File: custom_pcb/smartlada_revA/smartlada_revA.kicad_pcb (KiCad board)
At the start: 2 copper layers, 80 x 65 mm, 34 parts, among them J1 +12V IN, J2 LAMPS_OUT, J3 DEVBOARD PINS, Q1 AOD4184A, Q2 AOD4184A, Q3 AOD4184A, Q4 AOD4184A, Q5 AOD4185, U1 TPS54202DDC

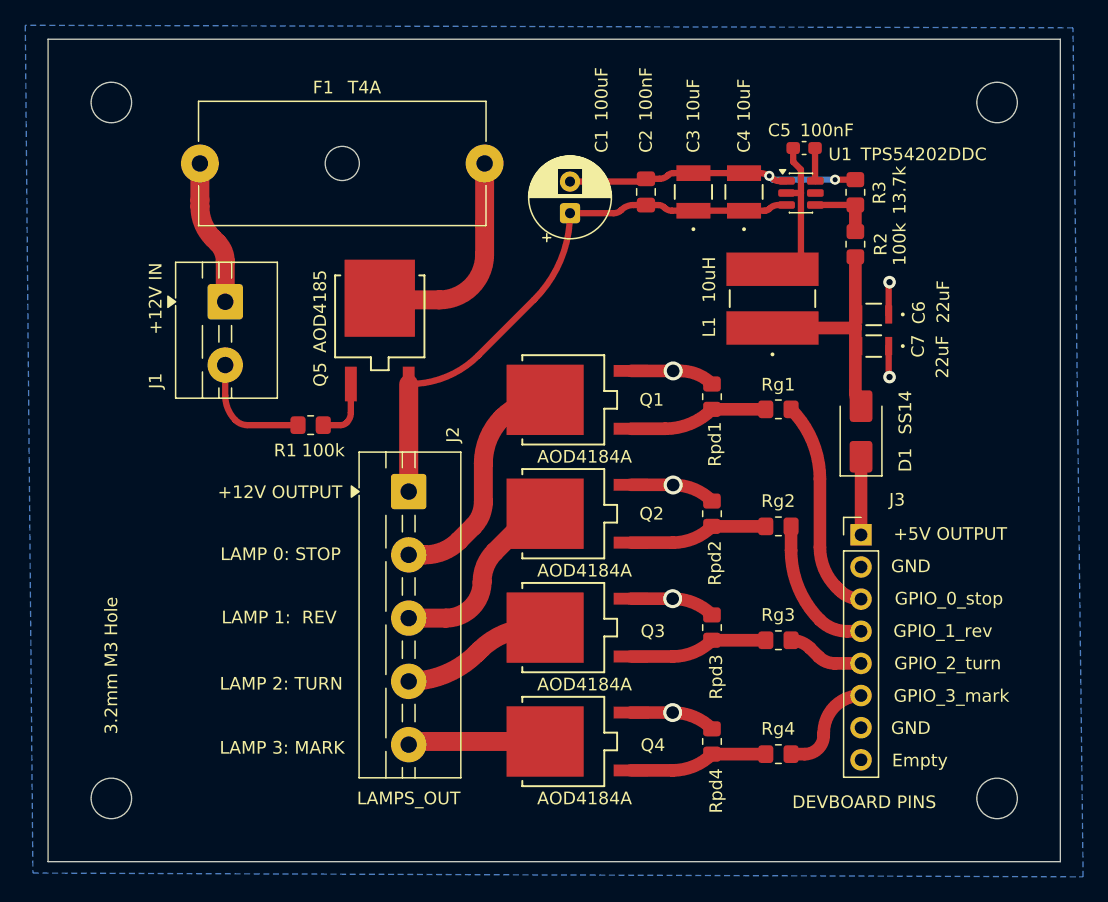
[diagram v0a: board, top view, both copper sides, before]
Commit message: Add Rev B/Rev C boards + firmware; repo hygiene
PCB: Rev C (product) routed/verified/gerbers/mechanical, ordered; Rev B
(learning 4-layer) + docs; Rev A updates; Vendor lib new footprints
(Faston TE_1217754-1, WS2812B, ESP32-C6-WROOM-1-N16, USB-B, tactile) + 3D shapes.

Firmware: SmartLadaRevC (fork of RevB with Rev C pin remap, builds;
PD-gating pending -> CODE_HANDOFF.md); SmartLadaRevB (modular UI, effects, fonts).

Docs/tooling: Rev C verification/procurement/handoffs, fab READMEs, KiCad
workflow, test sketches, tools; UI fonts limited to chosen orp/dweep.

Repo hygiene: .gitignore excludes timelapse video, payment docs, backups,
datasheets, renders, node_modules, unused font experiments.

Co-Authored-By: Claude Opus 4.8 <noreply@anthropic.com>
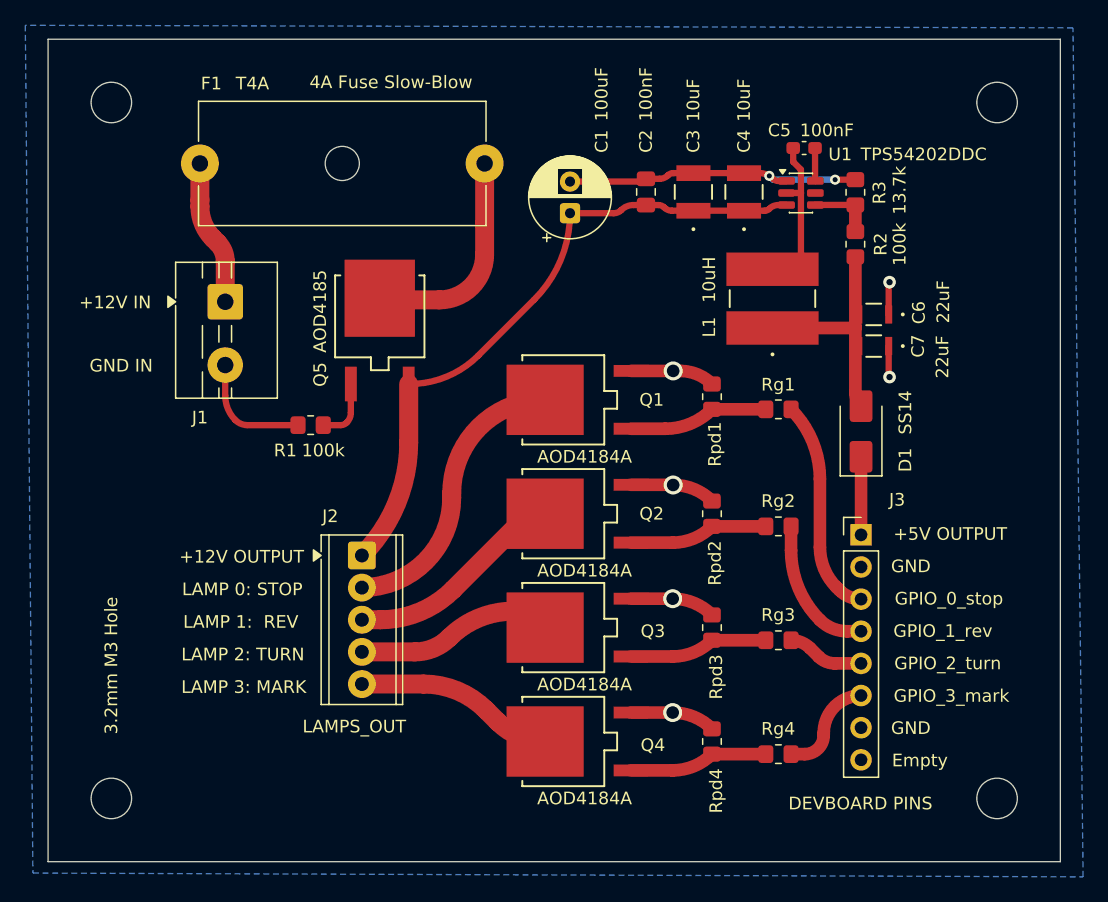
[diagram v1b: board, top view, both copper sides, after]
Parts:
- J2: footprint TerminalBlock:TerminalBlock_MaiXu_MX126-5.0-05P_1x05_P5.00mm -> TerminalBlock_Phoenix:TerminalBlock_Phoenix_MPT-0,5-5-2.54_1x05_P2.54mm_Horizontal
- moved J2 6.26 mm to (104.8, 83.3)
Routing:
- net +12V: track 45.9 -> 51.8 mm
- net /LAMP3: track 10.8 -> 15.8 mm
- net /LAMP2: track 11.9 -> 16.6 mm
- net /LAMP0: track 18.8 -> 22.5 mm
- net /LAMP1: track 15.2 -> 18.4 mm
